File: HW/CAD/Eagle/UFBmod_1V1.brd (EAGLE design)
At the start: 78.1 x 89.5 mm, 91 parts, among them U101 DIGILENT_CMOD_A7, U301 MAX5217, U401 AT86RF215-ZU, U411 ASVTX-13-D-26.000MHZ-I05-T, U511 PE4259, U521 RFX1010, U581 B39871B3440U410, U611 TPS62056DGSR, X221 TTE_EN11-HSM, X591 ANTENNATINY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

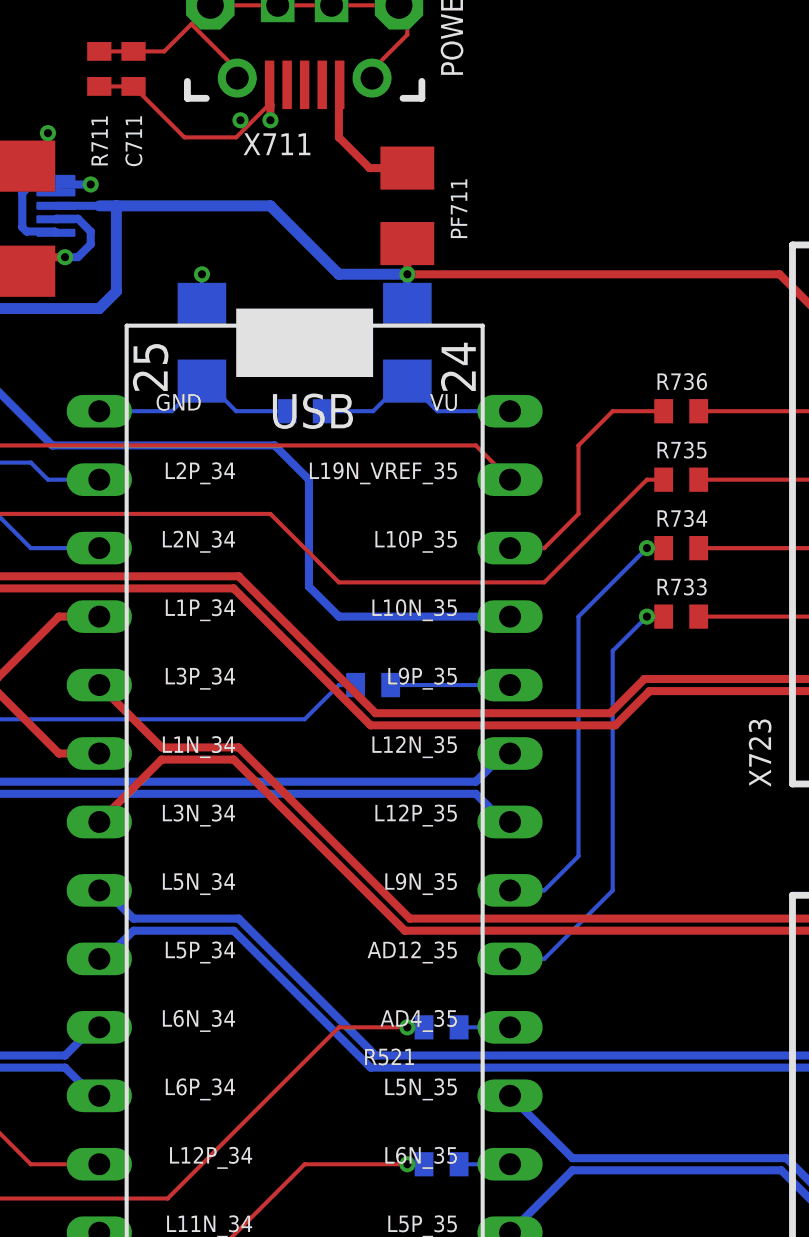
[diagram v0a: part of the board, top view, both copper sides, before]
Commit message: HW_1V1 - CAD/Eagle - LED resistors changed
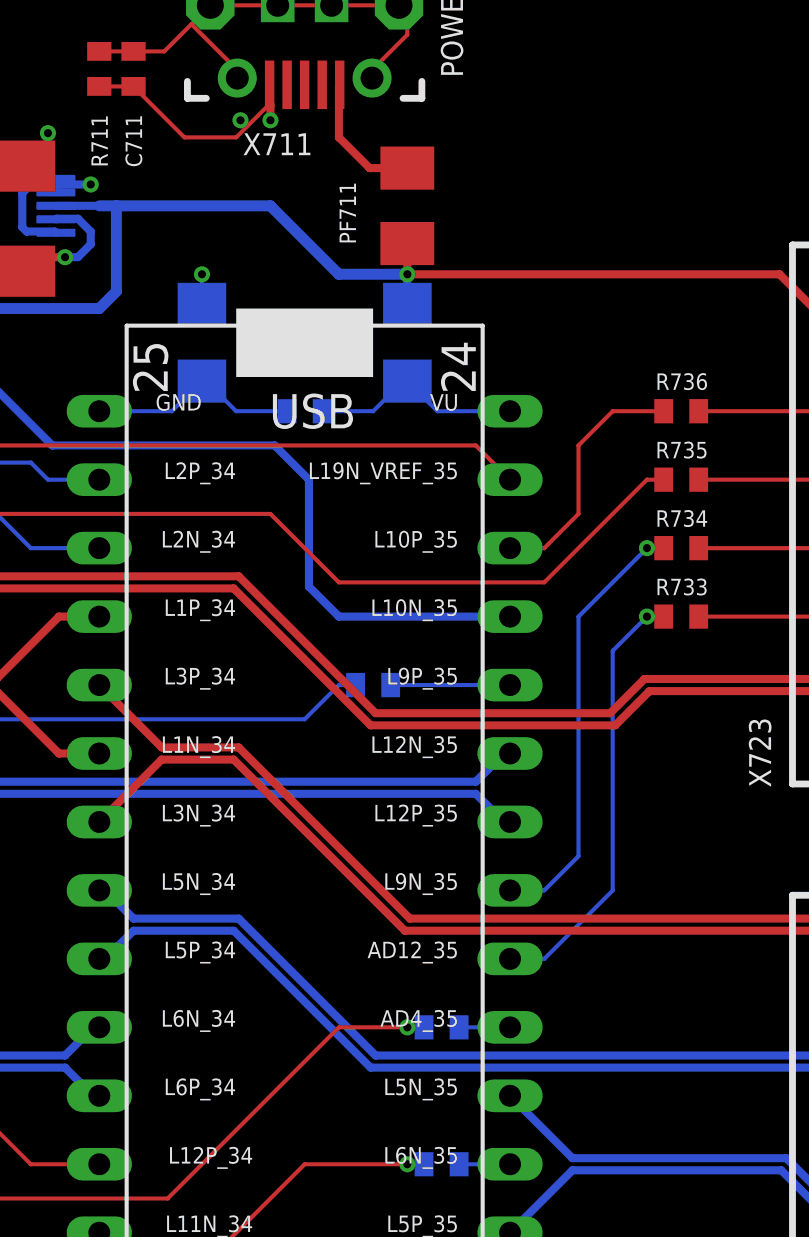
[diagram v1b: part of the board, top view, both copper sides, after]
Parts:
- R141: value 180R -> 820R
- R142: value 130R -> 1kR
- R143: value 130R -> 820R
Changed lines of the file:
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@@
 <layer number="49" name="Reference" color="7" fill="1" visible="yes" active="yes"/>
 <layer number="50" name="dxf" color="7" fill="1" visible="no" active="no"/>
-<layer number="51" name="tDocu" color="14" fill="1" visible="yes" active="yes"/>
-<layer number="52" name="bDocu" color="6" fill="1" visible="yes" active="yes"/>
+<layer number="51" name="tDocu" color="14" fill="1" visible="no" active="yes"/>
+<layer number="52" name="bDocu" color="6" fill="1" visible="no" active="yes"/>
 <layer number="53" name="tGND_GNDA" color="7" fill="9" visible="no" active="no"/>
 <layer number="54" name="bGND_GNDA" color="1" fill="9" visible="no" active="no"/>
@@
 </element>
 <element name="L101" library="df4iah_rcl" package="R1206" value="300R" x="49.53" y="74.93" smashed="yes" rot="MR270">
-<attribute name="NAME" x="51.1175" y="74.295" size="0.6096" layer="26" font="vector" rot="MR90"/>
+<attribute name="NAME" x="51.1175" y="73.9775" size="0.6096" layer="26" font="vector" rot="MR90"/>
 <attribute name="VALUE" x="52.07" y="76.2" size="1.27" layer="28" rot="MR270"/>
 </element>
 <element name="L102" library="df4iah_rcl" package="R1206" value="300R" x="41.91" y="74.93" smashed="yes" rot="MR270">
-<attribute name="NAME" x="43.4975" y="73.9775" size="0.6096" layer="26" font="vector" rot="MR90"/>
+<attribute name="NAME" x="40.005" y="75.8825" size="0.6096" layer="26" font="vector" rot="MR90"/>
 <attribute name="VALUE" x="44.45" y="76.2" size="1.27" layer="28" rot="MR270"/>
 </element>
@@
 </element>
 <element name="R131" library="df4iah_rcl" package="R0402" value="47R" x="48.26" y="62.23" smashed="yes" rot="MR180">
-<attribute name="NAME" x="49.2125" y="63.5" size="0.6096" layer="26" font="vector" ratio="10" rot="MR0"/>
+<attribute name="NAME" x="49.37125" y="63.1825" size="0.6096" layer="26" font="vector" ratio="10" rot="MR0"/>
 <attribute name="VALUE" x="46.6725" y="63.8175" size="0.6096" layer="28" font="vector" ratio="10" rot="MR180"/>
 </element>
@@
 </element>
 <element name="PF711" library="rcl" package="M1206" value="1.1A/2.2A" x="49.53" y="80.01" smashed="yes" rot="R90">
-<attribute name="NAME" x="51.7525" y="78.74" size="0.6096" layer="25" font="vector" rot="R90"/>
+<attribute name="NAME" x="47.625" y="78.58125" size="0.6096" layer="25" font="vector" rot="R90"/>
 <attribute name="VALUE" x="52.07" y="78.74" size="1.27" layer="27" rot="R90"/>
 </element>
@@
 <attribute name="VALUE" x="58.1025" y="63.1825" size="0.6096" layer="27" font="vector" ratio="10"/>
 </element>
-<element name="R141" library="df4iah_rcl" package="R0402" value="180R" x="55.88" y="34.29" smashed="yes" rot="R180">
+<element name="R141" library="df4iah_rcl" package="R0402" value="820R" x="55.88" y="34.29" smashed="yes" rot="R180">
 <attribute name="NAME" x="54.9275" y="35.08375" size="0.6096" layer="25" font="vector" ratio="10"/>
 <attribute name="VALUE" x="57.4675" y="35.8775" size="0.6096" layer="27" font="vector" ratio="10" rot="R180"/>
 </element>
-<element name="R142" library="df4iah_rcl" package="R0402" value="130R" x="55.88" y="36.83" smashed="yes" rot="R180">
+<element name="R142" library="df4iah_rcl" package="R0402" value="1kR" x="55.88" y="36.83" smashed="yes" rot="R180">
 <attribute name="NAME" x="54.9275" y="37.62375" size="0.6096" layer="25" font="vector" ratio="10"/>
 <attribute name="VALUE" x="57.4675" y="38.4175" size="0.6096" layer="27" font="vector" ratio="10" rot="R180"/>
 </element>
-<element name="R143" library="df4iah_rcl" package="R0402" value="130R" x="55.88" y="39.37" smashed="yes" rot="R180">
+<element name="R143" library="df4iah_rcl" package="R0402" value="820R" x="55.88" y="39.37" smashed="yes" rot="R180">
 <attribute name="NAME" x="54.9275" y="40.16375" size="0.6096" layer="25" font="vector" ratio="10"/>
 <attribute name="VALUE" x="57.4675" y="40.9575" size="0.6096" layer="27" font="vector" ratio="10" rot="R180"/>
@@
 <attribute name="VALUE" x="55.594" y="27.3362" size="1.27" layer="27"/>
 </element>
-<element name="R151" library="df4iah_rcl" package="R0402" value="1kR" x="50.8" y="29.21" rot="MR180"/>
-<element name="R152" library="df4iah_rcl" package="R0402" value="1kR" x="50.8" y="44.45" rot="MR180"/>
+<element name="R151" library="df4iah_rcl" package="R0402" value="1kR" x="50.8" y="29.21" smashed="yes" rot="MR180">
+<attribute name="NAME" x="51.59375" y="30.1625" size="0.6096" layer="26" font="vector" ratio="10" rot="MR0"/>
+<attribute name="VALUE" x="49.2125" y="30.7975" size="0.6096" layer="28" font="vector" ratio="10" rot="MR180"/>
+</element>
+<element name="R152" library="df4iah_rcl" package="R0402" value="1kR" x="50.8" y="44.45" smashed="yes" rot="MR180">
+<attribute name="NAME" x="51.59375" y="45.4025" size="0.6096" layer="26" font="vector" ratio="10" rot="MR0"/>
+<attribute name="VALUE" x="49.2125" y="46.0375" size="0.6096" layer="28" font="vector" ratio="10" rot="MR180"/>
+</element>
 <element name="X221" library="df4iah_switch" package="TTE_EN11-HSM" value="TTE_EN11-HSM" x="16.51" y="16.51" smashed="yes" rot="R90">
 <attribute name="NAME" x="24.67" y="9.635" size="0.8128" layer="25" ratio="20"/>
@@
 </element>
 <element name="R521" library="df4iah_rcl" package="R0402" value="1kR" x="50.8" y="49.53" smashed="yes" rot="MR180">
-<attribute name="NAME" x="49.8475" y="48.73625" size="0.6096" layer="25" font="vector" ratio="10" rot="R180"/>
+<attribute name="NAME" x="51.59375" y="50.4825" size="0.6096" layer="26" font="vector" ratio="10" rot="MR0"/>
 <attribute name="VALUE" x="49.2125" y="51.1175" size="0.6096" layer="28" font="vector" ratio="10" rot="MR180"/>
 </element>

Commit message: HW_1V1 - CAD/Eagle - LED wire names exchanged
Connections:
- net LED_B: now also R143.2, U101.11; no longer D141.6, R143.1
- net LED_B_R: now also D141.6, R143.1; no longer R143.2, U101.11
- net LED_G: now also R142.2, U101.10; no longer D141.5, R142.1
- net LED_G_R: now also D141.5, R142.1; no longer R142.2, U101.10
- net LED_R: now also R141.2, U101.9; no longer D141.4, R141.1
- net LED_R_R: now also D141.4, R141.1; no longer R141.2, U101.9
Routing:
- net LED_B_R: track 1.89 -> 9.98 mm
- net LED_B: track 9.98 -> 1.89 mm
- net LED_G_R: track 1.89 -> 8.65 mm
- net LED_G: track 8.65 -> 1.89 mm
- net LED_R_R: track 1.89 -> 7.32 mm
- net LED_R: track 7.32 -> 1.89 mm
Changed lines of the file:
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@@
 <wire x1="66.08" y1="64.77" x2="66.12" y2="64.81" width="0.1524" layer="1"/>
 </signal>
-<signal name="LED_G_R">
+<signal name="LED_G">
 <contactref element="U101" pad="10"/>
 <contactref element="R142" pad="2"/>
 <wire x1="53.34" y1="36.83" x2="55.23" y2="36.83" width="0.1524" layer="1"/>
 </signal>
-<signal name="LED_B_R">
+<signal name="LED_B">
 <contactref element="U101" pad="11"/>
 <contactref element="R143" pad="2"/>
 <wire x1="53.34" y1="39.37" x2="55.23" y2="39.37" width="0.1524" layer="1"/>
 </signal>
-<signal name="LED_R">
+<signal name="LED_R_R">
 <contactref element="R141" pad="1"/>
 <contactref element="D141" pad="4"/>
@@
 <wire x1="57.94375" y1="32.87625" x2="56.53" y2="34.29" width="0.1524" layer="1"/>
 </signal>
-<signal name="LED_G">
+<signal name="LED_G_R">
 <contactref element="R142" pad="1"/>
 <contactref element="D141" pad="5"/>
@@
 <wire x1="58.42" y1="34.94" x2="56.53" y2="36.83" width="0.1524" layer="1"/>
 </signal>
-<signal name="LED_B">
+<signal name="LED_B_R">
 <contactref element="R143" pad="1"/>
 <contactref element="D141" pad="6"/>
@@
 <wire x1="53.34" y1="29.21" x2="51.45" y2="29.21" width="0.1524" layer="16"/>
 </signal>
-<signal name="LED_R_R">
+<signal name="LED_R">
 <contactref element="U101" pad="9"/>
 <contactref element="R141" pad="2"/>
